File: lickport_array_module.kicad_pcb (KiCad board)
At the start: 2 copper layers, 203.2 x 147.3 mm, 189 parts, among them P1 PWR_JACK_2.5x5.5_SMD_VERT, P10 RECEPTACLE_2MM, P11 RECEPTACLE_2MM, P12 RECEPTACLE_2MM, P13 RECEPTACLE_2MM, P14 RECEPTACLE_2MM, P2 BNC, P3 RECEPTACLE_2MM, P4 RECEPTACLE_2MM, P5 RECEPTACLE_2MM, P6 RECEPTACLE_2MM, P7 RECEPTACLE_2MM, P8 RECEPTACLE_2MM, P9 RECEPTACLE_2MM, T1 TERM_BLK_ANG_2_PIN_3.5MM_PITCH, T10 TERM_BLK_ANG_2_PIN_3.5MM_PITCH, T11 TERM_BLK_ANG_2_PIN_3.5MM_PITCH, T12 TERM_BLK_ANG_2_PIN_3.5MM_PITCH, T2 TERM_BLK_ANG_2_PIN_3.5MM_PITCH, T3 TERM_BLK_ANG_2_PIN_3.5MM_PITCH, T4 TERM_BLK_ANG_2_PIN_3.5MM_PITCH, T5 TERM_BLK_ANG_2_PIN_3.5MM_PITCH, T6 TERM_BLK_ANG_2_PIN_3.5MM_PITCH, T7 TERM_BLK_ANG_2_PIN_3.5MM_PITCH, T8 TERM_BLK_ANG_2_PIN_3.5MM_PITCH, T9 TERM_BLK_ANG_2_PIN_3.5MM_PITCH, U1 AT42QT2120-MMHR, U10 DRV103, U11 DRV103, U12 DRV103, U13 DRV103, U2 DRV103, U3 DRV103, U4 DRV103, U5 DRV103, U6 DRV103, U7 DRV103, U8 DRV103, U9 DRV103

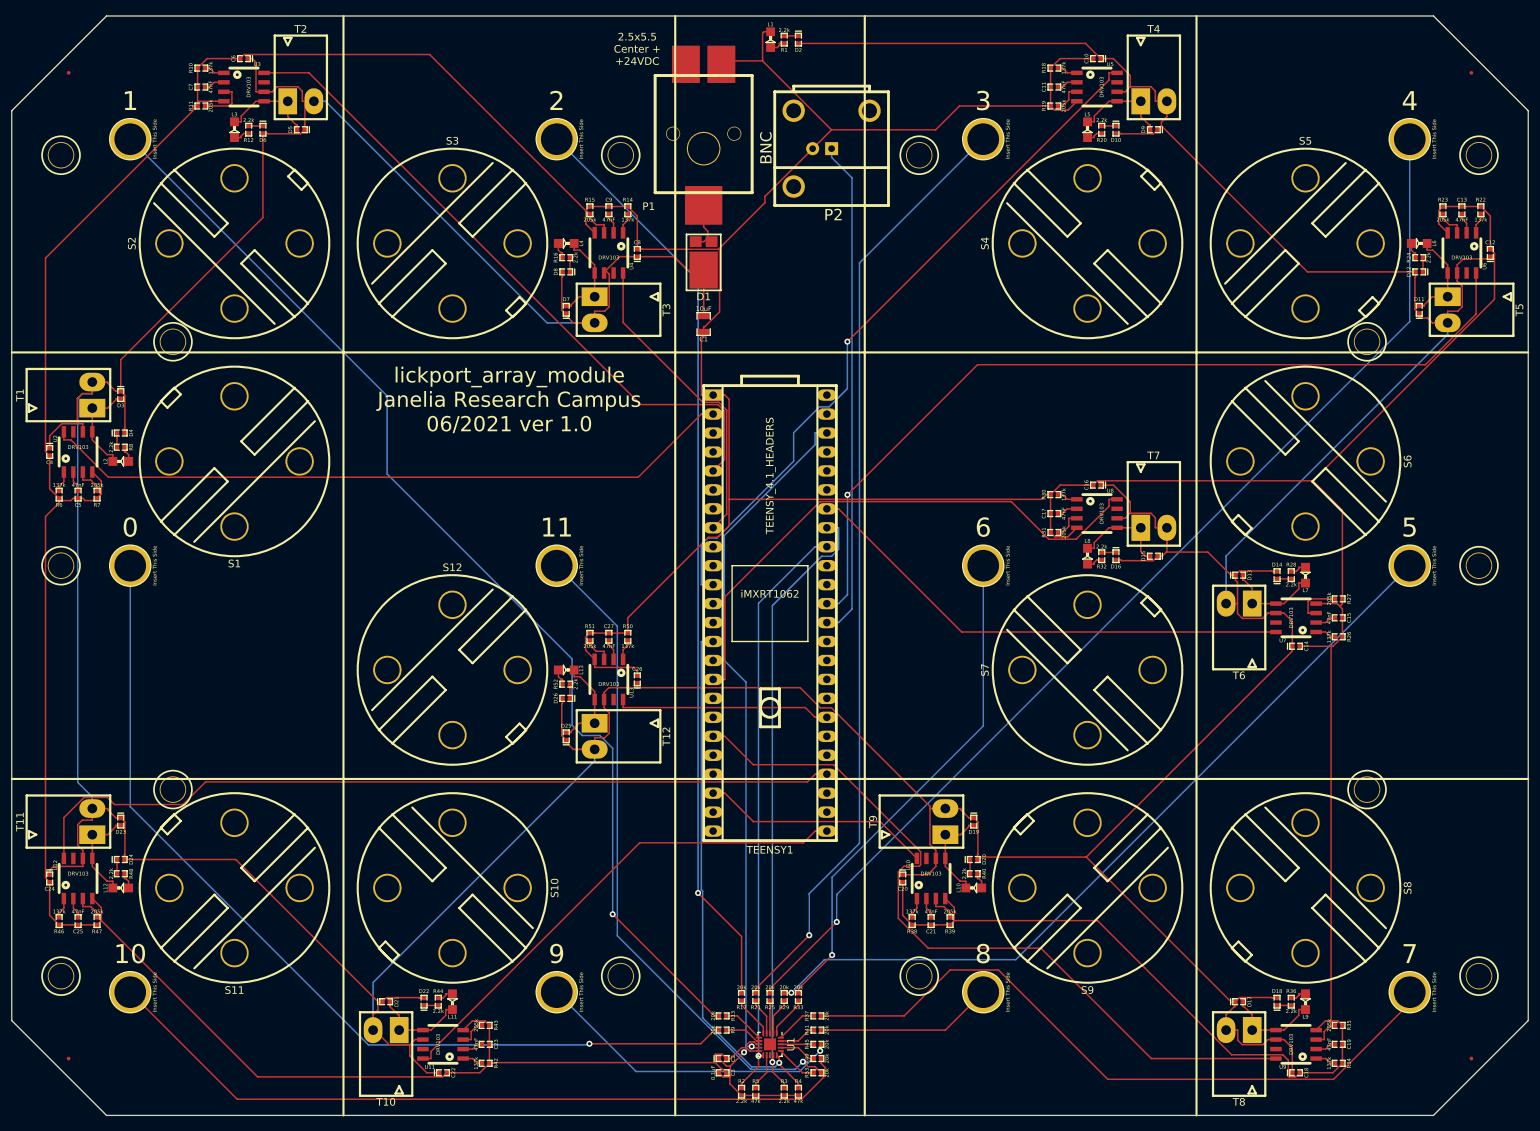
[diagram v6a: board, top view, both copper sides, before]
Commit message: Switch from Teensy 4.1 to Teensy 4.0 and hand route sense tracks
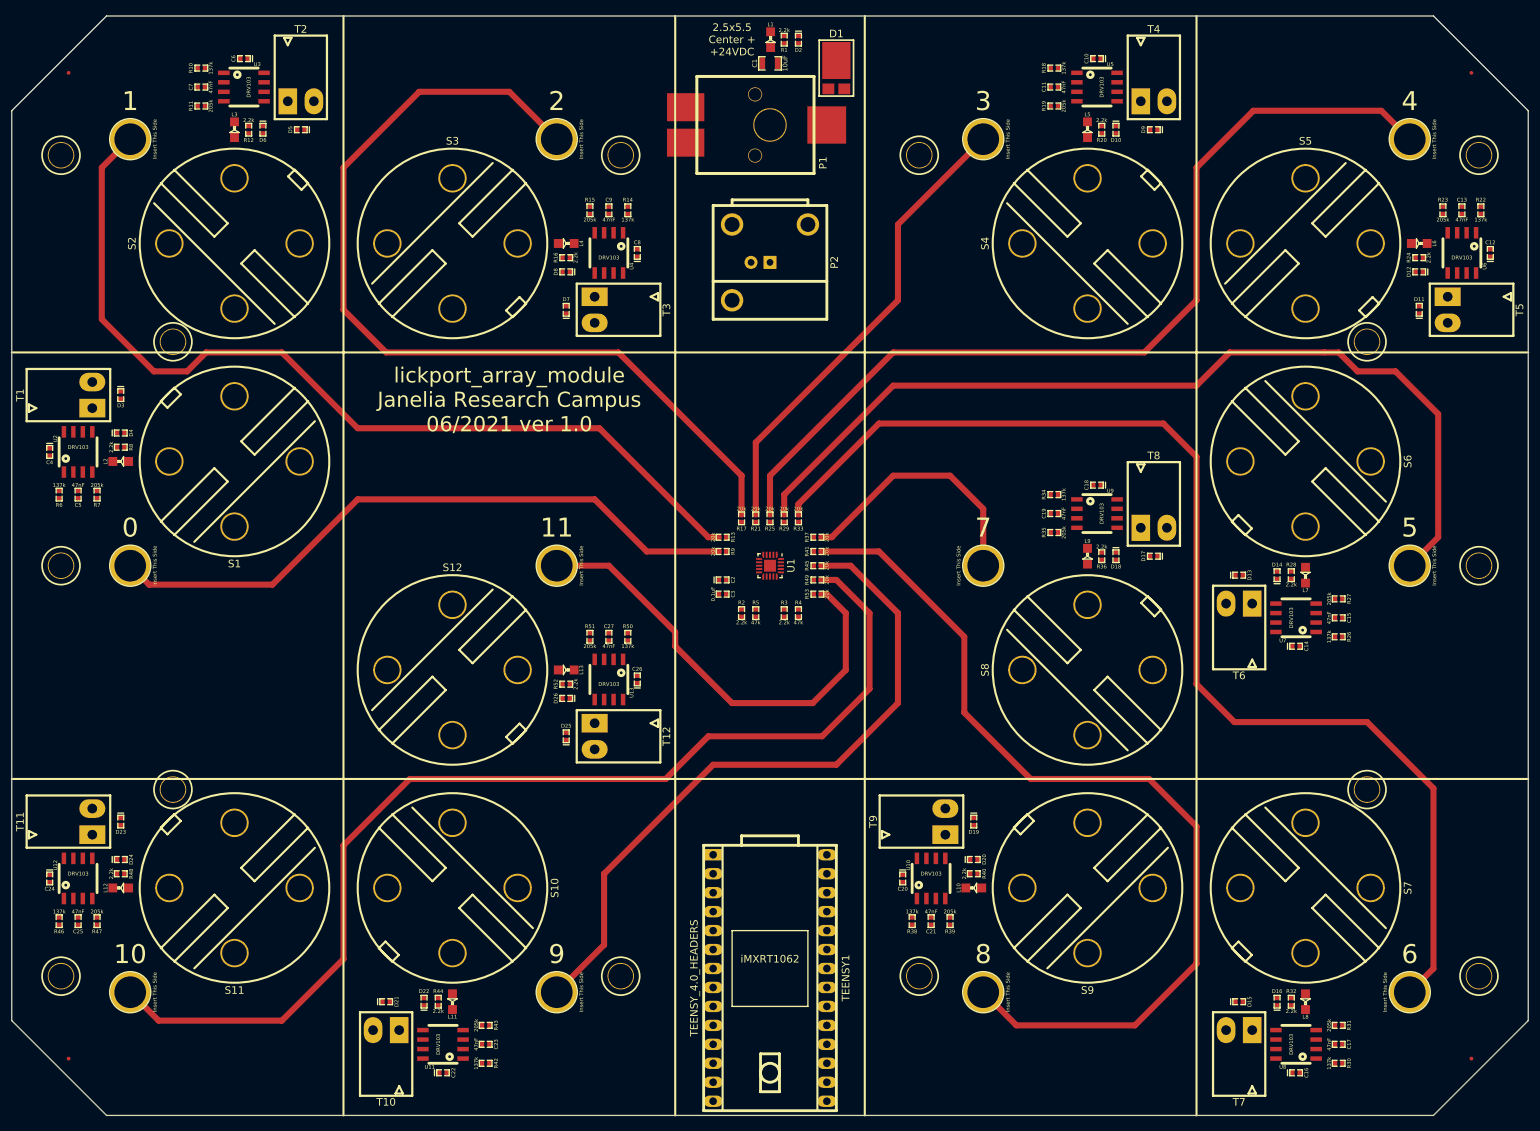
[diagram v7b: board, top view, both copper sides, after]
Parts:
- TEENSY1: value TEENSY_4.1_HEADERS -> TEENSY_4.0_HEADERS; footprint lickport_array_module:TEENSY_4.1_HEADERS -> lickport_array_module:TEENSY_4.0_HEADERS
- moved R30 85.2 mm to (215.9, 155.6), turned to 90 degrees
- moved R34 85.2 mm to (177.8, 79.4), turned to 270 degrees
- moved C16 83.1 mm to (210.2, 156.8), turned to 90 degrees
- moved C18 83.1 mm to (183.5, 78.1), turned to 270 degrees
- moved P10 80.8 mm to (168.3, 88.9), turned to 180 degrees
- moved P9 80.8 mm to (225.4, 146.1), turned to 180 degrees
- moved C17 80.7 mm to (215.9, 153.0), turned to 90 degrees
- moved C19 80.7 mm to (177.8, 81.9), turned to 270 degrees
- moved R31 76.2 mm to (215.9, 150.5), turned to 90 degrees
- moved R35 76.2 mm to (177.8, 84.5), turned to 270 degrees
- moved U8 76.0 mm to (210.2, 153.0), turned to 180 degrees
- moved U9 76.0 mm to (183.5, 81.9), turned to 0 degrees
- moved T7 68.3 mm to (202.6, 151.1), turned to 180 degrees
- moved T8 68.3 mm to (191.1, 83.8), turned to 0 degrees
- moved L8 66.5 mm to (211.5, 147.3), turned to 180 degrees
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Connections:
- net Net-(P10-Pad1) renamed /lickport_interface_7/SENSE
- net Net-(P11-Pad1) renamed /lickport_interface_8/SENSE
- net Net-(P12-Pad1) renamed /lickport_interface_9/SENSE
- net Net-(P13-Pad1) renamed /lickport_interface_10/SENSE
- net Net-(P14-Pad1) renamed /lickport_interface_11/SENSE
- net Net-(P3-Pad1) renamed /lickport_interface_0/SENSE
- net Net-(P4-Pad1) renamed /lickport_interface_1/SENSE
- net Net-(P5-Pad1) renamed /lickport_interface_2/SENSE
- net Net-(P6-Pad1) renamed /lickport_interface_3/SENSE
- net Net-(P7-Pad1) renamed /lickport_interface_4/SENSE
- net Net-(P8-Pad1) renamed /lickport_interface_5/SENSE
- net Net-(P9-Pad1) renamed /lickport_interface_6/SENSE
- TEENSY1 pad 1: (no net) -> /SOLENOID_1
- TEENSY1 pad 10: (no net) -> /SOLENOID_10
- TEENSY1 pad 11: (no net) -> /SOLENOID_11
- TEENSY1 pad 15: /SOLENOID_4 -> (no net)
- TEENSY1 pad 2: (no net) -> /SOLENOID_2
- TEENSY1 pad 20: /SOLENOID_5 -> (no net)
- TEENSY1 pad 3: /SOLENOID_1 -> /SOLENOID_3
- TEENSY1 pad 4: (no net) -> /SOLENOID_4
- TEENSY1 pad 5: (no net) -> /SOLENOID_5
- TEENSY1 pad 6: /SOLENOID_2 -> /SOLENOID_6
- TEENSY1 pad 7: (no net) -> /SOLENOID_7
- TEENSY1 pad 8: (no net) -> /SOLENOID_8
- TEENSY1 pad 9: /SOLENOID_3 -> /SOLENOID_9
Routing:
- net GND: track 837.2 -> 0.00 mm
- net VCC: track 832.7 -> 0.00 mm
- net /SOLENOID_4: track 116.4 -> 0.00 mm, vias 1 -> 0
- net VDD: track 112.7 -> 0.00 mm, vias 2 -> 0
- net /SOLENOID_10: track 110.9 -> 0.00 mm
- net /SOLENOID_7: track 104.0 -> 0.00 mm
- net /lickport_interface_8/SENSE: track 23.8 -> 123.8 mm
- net /SOLENOID_3: track 95.3 -> 0.00 mm, vias 1 -> 0
- net /SOLENOID_0: track 93.7 -> 0.00 mm
- net /lickport_interface_6/SENSE: track 67.6 -> 157.7 mm, vias 1 -> 0
- net /SOLENOID_1: track 89.1 -> 0.00 mm
- net /SCL: track 82.7 -> 0.00 mm, vias 1 -> 0
- net /SDA: track 78.9 -> 0.00 mm, vias 1 -> 0
- net /SOLENOID_6: track 75.3 -> 0.00 mm
- net /~CHANGE: track 70.9 -> 0.00 mm, vias 1 -> 0
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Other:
- net class SENSE added: clearance 0.2032, trace_width 0.8128, via_dia 0.9144, via_drill 0.6096

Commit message: Update net classes
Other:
- net class HIGHPOWER added: clearance 0.2032, trace_width 0.6096, via_dia 0.6096, via_drill 0.4064
